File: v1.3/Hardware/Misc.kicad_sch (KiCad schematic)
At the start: 20 parts, among them J6 DS1069-04MVW6X, J7 DS1069-02MVW6X, J8 DS1069-04MVW6X, Q18 MMBT3904, Q19 MMBT3904, Q20 MMBT3904, U15 4N25, U16 ADM2483xRW

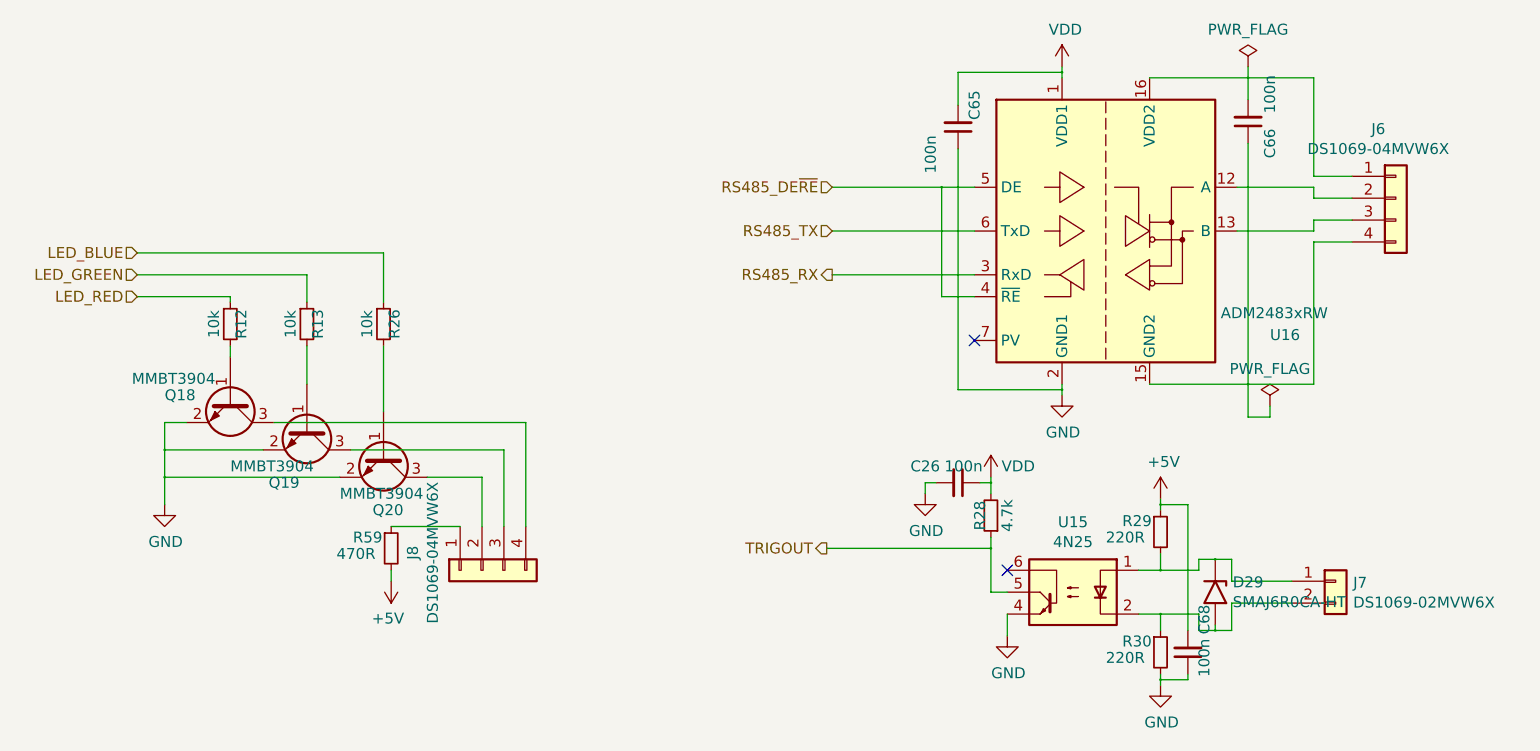
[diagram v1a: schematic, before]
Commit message: v1.3 Schematic, footprints and BOM updated.
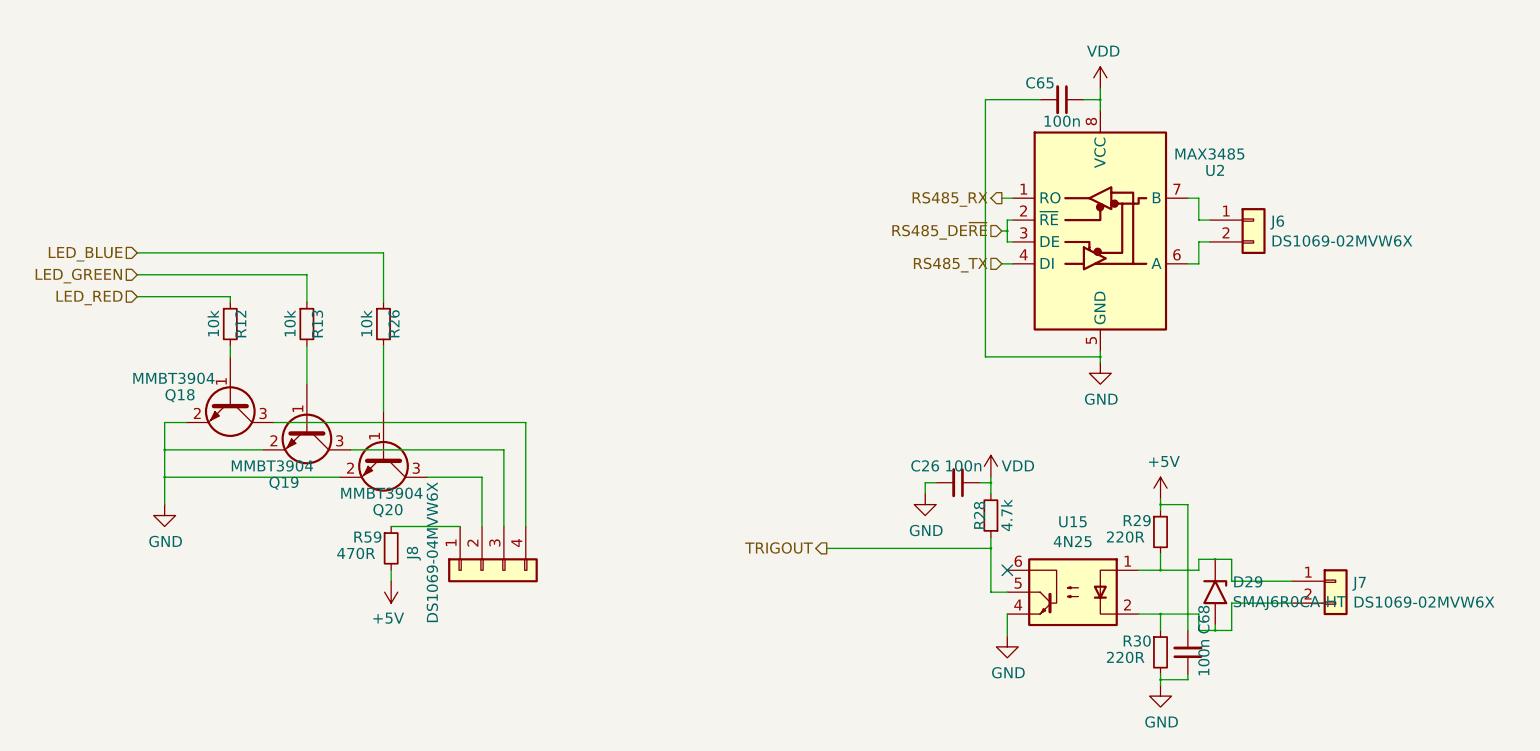
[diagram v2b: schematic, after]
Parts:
- removed C66: 100n, Capacitor_SMD:C_0805_2012Metric, symbol Device:C_Small
- removed J6: DS1069-04MVW6X, Connector_JST:JST_EH_B4B-EH-A_1x04_P2.50mm_Vertical, symbol Connector_Generic:Conn_01x04
- removed U16: ADM2483xRW, Package_SO:SOIC-16W_7.5x10.3mm_P1.27mm, symbol Interface_UART:ADM2483xRW
- added J6: DS1069-02MVW6X, Connector_JST:JST_EH_B2B-EH-A_1x02_P2.50mm_Vertical, symbol Connector_Generic:Conn_01x02
- added U2: MAX3485, Package_SO:SOIC-8_3.9x4.9mm_P1.27mm, symbol Interface_UART:MAX3485
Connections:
- net GND: now also C65.2, U2.5 (GND); no longer C65.1
- net RS485_DE~RE: now also U2.2 (~RE), U2.3 (DE)
- net RS485_RX: now also U2.1 (RO)
- net RS485_TX: now also U2.4 (DI)
- net VDD: now also C65.1, U2.8 (VCC); no longer C65.2
- new net: J6.2 (Pin_2), U2.6 (A)
- new net: J6.1 (Pin_1), U2.7 (B)
- no-connect marks 2 -> 1
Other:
- moved on the sheet: C65

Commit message: v1.3 Layout added & schematic update.
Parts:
- removed C26: 100n, Capacitor_SMD:C_0805_2012Metric, symbol Device:C_Small
- removed U2: MAX3485, Package_SO:SOIC-8_3.9x4.9mm_P1.27mm, symbol Interface_UART:MAX3485
- added Q4: MMBT3904, Package_TO_SOT_SMD:SOT-23, symbol Transistor_BJT:MMBT3904
- added R10: 10k, Resistor_SMD:R_0805_2012Metric, symbol Device:R_Small
- added R27: 120R, Resistor_SMD:R_0805_2012Metric, symbol Device:R_Small
- added R4: 4.7k, Resistor_SMD:R_0805_2012Metric, symbol Device:R_Small
- added U2: ADM485, Package_SO:SOIC-8_3.9x4.9mm_P1.27mm, symbol Interface_UART:MAX485E
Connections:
- net +5V: now also C65.1, U2.8 (VCC)
- net GND: now also U2.5 (GND)
- net RS485_DE~RE: now also U2.2 (~RE), U2.3 (DE)
- net RS485_RX: now also Q4.3 (C), R4.1
- net RS485_TX: now also U2.4 (DI)
- net VDD: now also R10.1, R4.2; no longer C65.1
- net at J6.2 (Pin_2): now also R27.2, U2.6 (A)
- net at J6.1 (Pin_1): now also R27.1, U2.7 (B)
- new net: Q4.1 (B), R10.2
- new net: Q4.2 (E), U2.1 (RO)
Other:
- moved on the sheet: J6
